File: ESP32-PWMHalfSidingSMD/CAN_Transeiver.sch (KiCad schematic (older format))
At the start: 13 parts, among them J1 RJ45, J2 RJ45, T1 + 15 in -, T2 + 15 out -, U1 TCAN332DR

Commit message: Update part numbers for ESP32-PWMHalfSidingSMD and created prelim BOM files.
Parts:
- R1, R2: Mouser Part Number 71-RN60C60R0B/R -> 71-CRCW120660R0KNAIF
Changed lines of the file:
@@
 F 2 "~" V 5780 3650 30  0000 C CNN
 F 3 "~" H 5850 3650 30  0000 C CNN
-F 4 " 71-RN60C60R0B/R" H 5850 3650 60  0001 C CNN "Mouser Part Number"
+F 4 "71-CRCW120660R0KNAIF " H 5850 3650 60  0001 C CNN "Mouser Part Number"
 	1    5850 3650
 	1    0    0    -1
@@
 F 2 "~" V 6480 3650 30  0000 C CNN
 F 3 "~" H 6550 3650 30  0000 C CNN
-F 4 " 71-RN60C60R0B/R" H 6550 3650 60  0001 C CNN "Mouser Part Number"
+F 4 "71-CRCW120660R0KNAIF " H 6550 3650 60  0001 C CNN "Mouser Part Number"
 	1    6550 3650
 	1    0    0    -1

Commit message: Updated ESP32-PWMHalfSidingSMD board.
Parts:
- C1, C3: footprint ~ -> Capacitors_SMD:C_0603; symbol C -> C-RESCUE-ESP32-PWMHalfSidingSMD
- C2: footprint ~ -> Capacitors_SMD:CP_Elec_4x5.7; symbol CP1 -> CP1-RESCUE-ESP32-PWMHalfSidingSMD
- D1, D2: footprint ~ -> Diodes_SMD:D_SMB
- J1, J2: footprint (none) -> RJ45-8N-S:RJ45_8N-S
- JP1: footprint (none) -> Pin_Headers:Pin_Header_Straight_2x02_Pitch2.54mm
- R1, R2: footprint ~ -> Resistors_SMD:R_1206; symbol R -> R-RESCUE-ESP32-PWMHalfSidingSMD
- T1, T2: footprint (none) -> Connectors_Terminal_Blocks:TerminalBlock_Pheonix_MPT-2.54mm_2pol
- U1: footprint ~ -> Housings_SOIC:SOIC-8_3.9x4.9mm_Pitch1.27mm
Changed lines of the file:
@@
 EESchema Schematic File Version 2
+LIBS:ESP32-PWMHalfSidingSMD-rescue
 LIBS:power
 LIBS:device
@@
 LIBS:memory
 LIBS:xilinx
-LIBS:special
 LIBS:microcontrollers
 LIBS:dsp
@@
 LIBS:4814p-2
 LIBS:ESP32-PWMHalfSidingSMD-cache
-EELAYER 27 0
+EELAYER 25 0
 EELAYER END
 $Descr A4 11693 8268
@@
 F 0 "U1" H 4100 3350 30  0000 C CNN
 F 1 "TCAN332DR" H 4100 3450 30  0000 C CNN
-F 2 "~" H 4100 3400 60  0000 C CNN
+F 2 "Housings_SOIC:SOIC-8_3.9x4.9mm_Pitch1.27mm" H 4100 3400 60  0001 C CNN
 F 3 "~" H 4100 3400 60  0000 C CNN
 F 4 "595-TCAN332DR" H 4100 3400 60  0001 C CNN "Mouser Part Number"
@@
 $EndComp
 $Comp
-L GND #PWR011
+L GND-RESCUE-ESP32-PWMHalfSidingSMD #PWR011
 U 1 1 5C828CBC
 P 4100 3800
@@
 	3750 3300 3750 4400
 $Comp
-L C C1
+L C-RESCUE-ESP32-PWMHalfSidingSMD C1
 U 1 1 5C828DA1
 P 4650 3800
+AR Path="/5C828DA1" Ref="C1"  Part="1"
+AR Path="/5C828AE5/5C828DA1" Ref="C1"  Part="1"
 F 0 "C1" H 4650 3900 40  0000 L CNN
 F 1 ".1 uf" H 4656 3715 40  0000 L CNN
-F 2 "~" H 4688 3650 30  0000 C CNN
+F 2 "Capacitors_SMD:C_0603" H 4688 3650 30  0001 C CNN
 F 3 "~" H 4650 3800 60  0000 C CNN
 F 4 "710-885012206095" H 4650 3800 60  0001 C CNN "Mouser Part Number"
@@
 $EndComp
 $Comp
-L CP1 C2
+L CP1-RESCUE-ESP32-PWMHalfSidingSMD C2
 U 1 1 5C828DB0
 P 5000 3800
 F 0 "C2" H 5050 3900 50  0000 L CNN
 F 1 "15 uf 15V" H 5050 3700 50  0000 L CNN
-F 2 "~" H 5000 3800 60  0000 C CNN
+F 2 "Capacitors_SMD:CP_Elec_4x5.7" H 5000 3800 60  0001 C CNN
 F 3 "~" H 5000 3800 60  0000 C CNN
 F 4 "647-UUD1C150MCL" H 5000 3800 60  0001 C CNN "Mouser Part Number"
@@
 CANL
 $Comp
-L R R1
+L R-RESCUE-ESP32-PWMHalfSidingSMD R1
 U 1 1 5C828F93
 P 5850 3650
 F 0 "R1" V 5930 3650 40  0000 C CNN
 F 1 "60 Ohms" V 5857 3651 40  0000 C CNN
-F 2 "~" V 5780 3650 30  0000 C CNN
+F 2 "Resistors_SMD:R_1206" V 5780 3650 30  0001 C CNN
 F 3 "~" H 5850 3650 30  0000 C CNN
 F 4 "71-CRCW120660R0KNAIF " H 5850 3650 60  0001 C CNN "Mouser Part Number"
@@
 $EndComp
 $Comp
-L R R2
+L R-RESCUE-ESP32-PWMHalfSidingSMD R2
 U 1 1 5C828FA2
 P 6550 3650
 F 0 "R2" V 6630 3650 40  0000 C CNN
 F 1 "60 Ohms" V 6557 3651 40  0000 C CNN
-F 2 "~" V 6480 3650 30  0000 C CNN
+F 2 "Resistors_SMD:R_1206" V 6480 3650 30  0001 C CNN
 F 3 "~" H 6550 3650 30  0000 C CNN
 F 4 "71-CRCW120660R0KNAIF " H 6550 3650 60  0001 C CNN "Mouser Part Number"
@@
 F 0 "JP1" H 6200 4350 50  0000 C CNN
 F 1 "Termination" H 6210 4070 40  0000 C CNN
-F 2 "" H 6200 4200 60  0000 C CNN
+F 2 "Pin_Headers:Pin_Header_Straight_2x02_Pitch2.54mm" H 6200 4200 60  0001 C CNN
 F 3 "" H 6200 4200 60  0000 C CNN
 F 4 "649-67997-404HLF" H 6200 4200 60  0001 C CNN "Mouser Part Number"
@@
 	6700 4150 6600 4150
 $Comp
-L C C3
+L C-RESCUE-ESP32-PWMHalfSidingSMD C3
 U 1 1 5C8290C3
 P 6200 4750
+AR Path="/5C8290C3" Ref="C3"  Part="1"
+AR Path="/5C828AE5/5C8290C3" Ref="C3"  Part="1"
 F 0 "C3" H 6200 4850 40  0000 L CNN
 F 1 "47 nf" H 6206 4665 40  0000 L CNN
-F 2 "~" H 6238 4600 30  0000 C CNN
+F 2 "Capacitors_SMD:C_0603" H 6238 4600 30  0000 C CNN
 F 3 "~" H 6200 4750 60  0000 C CNN
 F 4 "710-885012206093" H 6200 4750 60  0001 C CNN "Mouser Part Number"
@@
 $EndComp
 $Comp
-L GND #PWR012
+L GND-RESCUE-ESP32-PWMHalfSidingSMD #PWR012
 U 1 1 5C8290D2
 P 6200 5100
@@
 F 0 "J2" H 8550 5200 60  0000 C CNN
 F 1 "RJ45" H 8200 5200 60  0000 C CNN
-F 2 "" H 8350 4700 60  0000 C CNN
+F 2 "RJ45-8N-S:RJ45_8N-S" H 8350 4700 60  0001 C CNN
 F 3 "" H 8350 4700 60  0000 C CNN
 F 4 "710-615008144221" H 8350 4700 60  0001 C CNN "Mouser Part Number"
@@
 F 0 "J1" H 8550 3550 60  0000 C CNN
 F 1 "RJ45" H 8200 3550 60  0000 C CNN
-F 2 "" H 8350 3050 60  0000 C CNN
+F 2 "RJ45-8N-S:RJ45_8N-S" H 8350 3050 60  0001 C CNN
 F 3 "" H 8350 3050 60  0000 C CNN
 F 4 "710-615008144221" H 8350 3050 60  0001 C CNN "Mouser Part Number"
@@
 F 0 "T2" V 6750 2050 40  0000 C CNN
 F 1 "+ 15 out -" V 6850 2050 40  0000 C CNN
-F 2 "" H 6800 2050 60  0000 C CNN
+F 2 "Connectors_Terminal_Blocks:TerminalBlock_Pheonix_MPT-2.54mm_2pol" H 6800 2050 60  0001 C CNN
 F 3 "" H 6800 2050 60  0000 C CNN
 F 4 "651-1725656" H 6800 2050 60  0001 C CNN "Mouser Part Number"
@@
 F 0 "D2" H 6150 2050 40  0000 C CNN
 F 1 "DFLS240-7" H 6150 1850 40  0000 C CNN
-F 2 "~" H 6150 1950 60  0000 C CNN
+F 2 "Diodes_SMD:D_SMB" H 6150 1950 60  0001 C CNN
 F 3 "~" H 6150 1950 60  0000 C CNN
 F 4 "621-DFLS240-7" H 6150 1950 60  0001 C CNN "Mouser Part Number"
@@
 	7450 3000 7450 5050
 $Comp
-L GND #PWR013
+L GND-RESCUE-ESP32-PWMHalfSidingSMD #PWR013
 U 1 1 5C8295F7
 P 6750 2650
@@
 F 0 "T1" V 5800 1050 40  0000 C CNN
 F 1 "+ 15 in -" V 5900 1050 40  0000 C CNN
-F 2 "" H 5850 1050 60  0000 C CNN
+F 2 "Connectors_Terminal_Blocks:TerminalBlock_Pheonix_MPT-2.54mm_2pol" H 5850 1050 60  0001 C CNN
 F 3 "" H 5850 1050 60  0000 C CNN
 F 4 "651-1725656" H 5850 1050 60  0001 C CNN "Mouser Part Number"
@@
 F 0 "D1" H 5750 1750 40  0000 C CNN
 F 1 "DFLS240-7" H 5750 1550 40  0000 C CNN
-F 2 "~" H 5750 1650 60  0000 C CNN
+F 2 "Diodes_SMD:D_SMB" H 5750 1650 60  0001 C CNN
 F 3 "~" H 5750 1650 60  0000 C CNN
 F 4 "621-DFLS240-7" H 5750 1650 60  0001 C CNN "Mouser Part Number"
@@
 	3750 4400 3600 4400
 $Comp
-L GND #PWR014
+L GND-RESCUE-ESP32-PWMHalfSidingSMD #PWR014
 U 1 1 5C828CCB
 P 4100 4950

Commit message: Restore PocketBeagleCommandStation_SMD.kicad_pcb
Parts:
- C1, C3: footprint Capacitors_SMD:C_0603 -> ~; symbol C-RESCUE-ESP32-PWMHalfSidingSMD -> C
- C2: footprint Capacitors_SMD:CP_Elec_4x5.7 -> ~; symbol CP1-RESCUE-ESP32-PWMHalfSidingSMD -> CP1
- D1, D2: footprint Diodes_SMD:D_SMB -> ~
- J1, J2: footprint RJ45-8N-S:RJ45_8N-S -> (none)
- JP1: footprint Pin_Headers:Pin_Header_Straight_2x02_Pitch2.54mm -> (none)
- R1, R2: footprint Resistors_SMD:R_1206 -> ~; symbol R-RESCUE-ESP32-PWMHalfSidingSMD -> R
- T1, T2: footprint Connectors_Terminal_Blocks:TerminalBlock_Pheonix_MPT-2.54mm_2pol -> (none)
- U1: footprint Housings_SOIC:SOIC-8_3.9x4.9mm_Pitch1.27mm -> ~
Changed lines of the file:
@@
 EESchema Schematic File Version 2
-LIBS:ESP32-PWMHalfSidingSMD-rescue
 LIBS:power
 LIBS:device
@@
 LIBS:memory
 LIBS:xilinx
+LIBS:special
 LIBS:microcontrollers
 LIBS:dsp
@@
 LIBS:4814p-2
 LIBS:ESP32-PWMHalfSidingSMD-cache
-EELAYER 25 0
+EELAYER 27 0
 EELAYER END
 $Descr A4 11693 8268
@@
 F 0 "U1" H 4100 3350 30  0000 C CNN
 F 1 "TCAN332DR" H 4100 3450 30  0000 C CNN
-F 2 "Housings_SOIC:SOIC-8_3.9x4.9mm_Pitch1.27mm" H 4100 3400 60  0001 C CNN
+F 2 "~" H 4100 3400 60  0000 C CNN
 F 3 "~" H 4100 3400 60  0000 C CNN
 F 4 "595-TCAN332DR" H 4100 3400 60  0001 C CNN "Mouser Part Number"
@@
 $EndComp
 $Comp
-L GND-RESCUE-ESP32-PWMHalfSidingSMD #PWR011
+L GND #PWR011
 U 1 1 5C828CBC
 P 4100 3800
@@
 	3750 3300 3750 4400
 $Comp
-L C-RESCUE-ESP32-PWMHalfSidingSMD C1
+L C C1
 U 1 1 5C828DA1
 P 4650 3800
-AR Path="/5C828DA1" Ref="C1"  Part="1"
-AR Path="/5C828AE5/5C828DA1" Ref="C1"  Part="1"
 F 0 "C1" H 4650 3900 40  0000 L CNN
 F 1 ".1 uf" H 4656 3715 40  0000 L CNN
-F 2 "Capacitors_SMD:C_0603" H 4688 3650 30  0001 C CNN
+F 2 "~" H 4688 3650 30  0000 C CNN
 F 3 "~" H 4650 3800 60  0000 C CNN
 F 4 "710-885012206095" H 4650 3800 60  0001 C CNN "Mouser Part Number"
@@
 $EndComp
 $Comp
-L CP1-RESCUE-ESP32-PWMHalfSidingSMD C2
+L CP1 C2
 U 1 1 5C828DB0
 P 5000 3800
 F 0 "C2" H 5050 3900 50  0000 L CNN
 F 1 "15 uf 15V" H 5050 3700 50  0000 L CNN
-F 2 "Capacitors_SMD:CP_Elec_4x5.7" H 5000 3800 60  0001 C CNN
+F 2 "~" H 5000 3800 60  0000 C CNN
 F 3 "~" H 5000 3800 60  0000 C CNN
 F 4 "647-UUD1C150MCL" H 5000 3800 60  0001 C CNN "Mouser Part Number"
@@
 CANL
 $Comp
-L R-RESCUE-ESP32-PWMHalfSidingSMD R1
+L R R1
 U 1 1 5C828F93
 P 5850 3650
 F 0 "R1" V 5930 3650 40  0000 C CNN
 F 1 "60 Ohms" V 5857 3651 40  0000 C CNN
-F 2 "Resistors_SMD:R_1206" V 5780 3650 30  0001 C CNN
+F 2 "~" V 5780 3650 30  0000 C CNN
 F 3 "~" H 5850 3650 30  0000 C CNN
 F 4 "71-CRCW120660R0KNAIF " H 5850 3650 60  0001 C CNN "Mouser Part Number"
@@
 $EndComp
 $Comp
-L R-RESCUE-ESP32-PWMHalfSidingSMD R2
+L R R2
 U 1 1 5C828FA2
 P 6550 3650
 F 0 "R2" V 6630 3650 40  0000 C CNN
 F 1 "60 Ohms" V 6557 3651 40  0000 C CNN
-F 2 "Resistors_SMD:R_1206" V 6480 3650 30  0001 C CNN
+F 2 "~" V 6480 3650 30  0000 C CNN
 F 3 "~" H 6550 3650 30  0000 C CNN
 F 4 "71-CRCW120660R0KNAIF " H 6550 3650 60  0001 C CNN "Mouser Part Number"
@@
 F 0 "JP1" H 6200 4350 50  0000 C CNN
 F 1 "Termination" H 6210 4070 40  0000 C CNN
-F 2 "Pin_Headers:Pin_Header_Straight_2x02_Pitch2.54mm" H 6200 4200 60  0001 C CNN
+F 2 "" H 6200 4200 60  0000 C CNN
 F 3 "" H 6200 4200 60  0000 C CNN
 F 4 "649-67997-404HLF" H 6200 4200 60  0001 C CNN "Mouser Part Number"
@@
 	6700 4150 6600 4150
 $Comp
-L C-RESCUE-ESP32-PWMHalfSidingSMD C3
+L C C3
 U 1 1 5C8290C3
 P 6200 4750
-AR Path="/5C8290C3" Ref="C3"  Part="1"
-AR Path="/5C828AE5/5C8290C3" Ref="C3"  Part="1"
 F 0 "C3" H 6200 4850 40  0000 L CNN
 F 1 "47 nf" H 6206 4665 40  0000 L CNN
-F 2 "Capacitors_SMD:C_0603" H 6238 4600 30  0000 C CNN
+F 2 "~" H 6238 4600 30  0000 C CNN
 F 3 "~" H 6200 4750 60  0000 C CNN
 F 4 "710-885012206093" H 6200 4750 60  0001 C CNN "Mouser Part Number"
@@
 $EndComp
 $Comp
-L GND-RESCUE-ESP32-PWMHalfSidingSMD #PWR012
+L GND #PWR012
 U 1 1 5C8290D2
 P 6200 5100
@@
 F 0 "J2" H 8550 5200 60  0000 C CNN
 F 1 "RJ45" H 8200 5200 60  0000 C CNN
-F 2 "RJ45-8N-S:RJ45_8N-S" H 8350 4700 60  0001 C CNN
+F 2 "" H 8350 4700 60  0000 C CNN
 F 3 "" H 8350 4700 60  0000 C CNN
 F 4 "710-615008144221" H 8350 4700 60  0001 C CNN "Mouser Part Number"
@@
 F 0 "J1" H 8550 3550 60  0000 C CNN
 F 1 "RJ45" H 8200 3550 60  0000 C CNN
-F 2 "RJ45-8N-S:RJ45_8N-S" H 8350 3050 60  0001 C CNN
+F 2 "" H 8350 3050 60  0000 C CNN
 F 3 "" H 8350 3050 60  0000 C CNN
 F 4 "710-615008144221" H 8350 3050 60  0001 C CNN "Mouser Part Number"
@@
 F 0 "T2" V 6750 2050 40  0000 C CNN
 F 1 "+ 15 out -" V 6850 2050 40  0000 C CNN
-F 2 "Connectors_Terminal_Blocks:TerminalBlock_Pheonix_MPT-2.54mm_2pol" H 6800 2050 60  0001 C CNN
+F 2 "" H 6800 2050 60  0000 C CNN
 F 3 "" H 6800 2050 60  0000 C CNN
 F 4 "651-1725656" H 6800 2050 60  0001 C CNN "Mouser Part Number"
@@
 F 0 "D2" H 6150 2050 40  0000 C CNN
 F 1 "DFLS240-7" H 6150 1850 40  0000 C CNN
-F 2 "Diodes_SMD:D_SMB" H 6150 1950 60  0001 C CNN
+F 2 "~" H 6150 1950 60  0000 C CNN
 F 3 "~" H 6150 1950 60  0000 C CNN
 F 4 "621-DFLS240-7" H 6150 1950 60  0001 C CNN "Mouser Part Number"
@@
 	7450 3000 7450 5050
 $Comp
-L GND-RESCUE-ESP32-PWMHalfSidingSMD #PWR013
+L GND #PWR013
 U 1 1 5C8295F7
 P 6750 2650
@@
 F 0 "T1" V 5800 1050 40  0000 C CNN
 F 1 "+ 15 in -" V 5900 1050 40  0000 C CNN
-F 2 "Connectors_Terminal_Blocks:TerminalBlock_Pheonix_MPT-2.54mm_2pol" H 5850 1050 60  0001 C CNN
+F 2 "" H 5850 1050 60  0000 C CNN
 F 3 "" H 5850 1050 60  0000 C CNN
 F 4 "651-1725656" H 5850 1050 60  0001 C CNN "Mouser Part Number"
@@
 F 0 "D1" H 5750 1750 40  0000 C CNN
 F 1 "DFLS240-7" H 5750 1550 40  0000 C CNN
-F 2 "Diodes_SMD:D_SMB" H 5750 1650 60  0001 C CNN
+F 2 "~" H 5750 1650 60  0000 C CNN
 F 3 "~" H 5750 1650 60  0000 C CNN
 F 4 "621-DFLS240-7" H 5750 1650 60  0001 C CNN "Mouser Part Number"
@@
 	3750 4400 3600 4400
 $Comp
-L GND-RESCUE-ESP32-PWMHalfSidingSMD #PWR014
+L GND #PWR014
 U 1 1 5C828CCB
 P 4100 4950

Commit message: Repair ESP32-PWMHalfSidingSMD and generate POS file.
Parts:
- C1, C3: footprint ~ -> Capacitors_SMD:C_0603; symbol C -> C-RESCUE-ESP32-PWMHalfSidingSMD
- C2: footprint ~ -> Capacitors_SMD:CP_Elec_4x5.7; symbol CP1 -> CP1-RESCUE-ESP32-PWMHalfSidingSMD
- D1, D2: footprint ~ -> Diodes_SMD:D_SMB
- J1, J2: footprint (none) -> RJ45-8N-S:RJ45_8N-S
- JP1: footprint (none) -> Pin_Headers:Pin_Header_Angled_2x02_Pitch2.54mm
- R1, R2: footprint ~ -> Resistors_SMD:R_1206; symbol R -> R-RESCUE-ESP32-PWMHalfSidingSMD
- T1, T2: footprint (none) -> Connectors_Terminal_Blocks:TerminalBlock_Pheonix_MPT-2.54mm_2pol
- U1: footprint ~ -> (none)
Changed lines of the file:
@@
 EESchema Schematic File Version 2
+LIBS:ESP32-PWMHalfSidingSMD-rescue
 LIBS:power
 LIBS:device
@@
 LIBS:memory
 LIBS:xilinx
-LIBS:special
 LIBS:microcontrollers
 LIBS:dsp
@@
 LIBS:4814p-2
 LIBS:ESP32-PWMHalfSidingSMD-cache
-EELAYER 27 0
+EELAYER 25 0
 EELAYER END
 $Descr A4 11693 8268
@@
 F 0 "U1" H 4100 3350 30  0000 C CNN
 F 1 "TCAN332DR" H 4100 3450 30  0000 C CNN
-F 2 "~" H 4100 3400 60  0000 C CNN
+F 2 "" H 4100 3400 60  0001 C CNN
 F 3 "~" H 4100 3400 60  0000 C CNN
 F 4 "595-TCAN332DR" H 4100 3400 60  0001 C CNN "Mouser Part Number"
@@
 $EndComp
 $Comp
-L GND #PWR011
+L GND-RESCUE-ESP32-PWMHalfSidingSMD #PWR011
 U 1 1 5C828CBC
 P 4100 3800
@@
 	3750 3300 3750 4400
 $Comp
-L C C1
+L C-RESCUE-ESP32-PWMHalfSidingSMD C1
 U 1 1 5C828DA1
 P 4650 3800
+AR Path="/5C828DA1" Ref="C1"  Part="1"
+AR Path="/5C828AE5/5C828DA1" Ref="C1"  Part="1"
 F 0 "C1" H 4650 3900 40  0000 L CNN
 F 1 ".1 uf" H 4656 3715 40  0000 L CNN
-F 2 "~" H 4688 3650 30  0000 C CNN
+F 2 "Capacitors_SMD:C_0603" H 4688 3650 30  0001 C CNN
 F 3 "~" H 4650 3800 60  0000 C CNN
 F 4 "710-885012206095" H 4650 3800 60  0001 C CNN "Mouser Part Number"
@@
 $EndComp
 $Comp
-L CP1 C2
+L CP1-RESCUE-ESP32-PWMHalfSidingSMD C2
 U 1 1 5C828DB0
 P 5000 3800
 F 0 "C2" H 5050 3900 50  0000 L CNN
 F 1 "15 uf 15V" H 5050 3700 50  0000 L CNN
-F 2 "~" H 5000 3800 60  0000 C CNN
+F 2 "Capacitors_SMD:CP_Elec_4x5.7" H 5000 3800 60  0001 C CNN
 F 3 "~" H 5000 3800 60  0000 C CNN
 F 4 "647-UUD1C150MCL" H 5000 3800 60  0001 C CNN "Mouser Part Number"
@@
 CANL
 $Comp
-L R R1
+L R-RESCUE-ESP32-PWMHalfSidingSMD R1
 U 1 1 5C828F93
 P 5850 3650
 F 0 "R1" V 5930 3650 40  0000 C CNN
 F 1 "60 Ohms" V 5857 3651 40  0000 C CNN
-F 2 "~" V 5780 3650 30  0000 C CNN
+F 2 "Resistors_SMD:R_1206" V 5780 3650 30  0001 C CNN
 F 3 "~" H 5850 3650 30  0000 C CNN
 F 4 "71-CRCW120660R0KNAIF " H 5850 3650 60  0001 C CNN "Mouser Part Number"
@@
 $EndComp
 $Comp
-L R R2
+L R-RESCUE-ESP32-PWMHalfSidingSMD R2
 U 1 1 5C828FA2
 P 6550 3650
 F 0 "R2" V 6630 3650 40  0000 C CNN
 F 1 "60 Ohms" V 6557 3651 40  0000 C CNN
-F 2 "~" V 6480 3650 30  0000 C CNN
+F 2 "Resistors_SMD:R_1206" V 6480 3650 30  0001 C CNN
 F 3 "~" H 6550 3650 30  0000 C CNN
 F 4 "71-CRCW120660R0KNAIF " H 6550 3650 60  0001 C CNN "Mouser Part Number"
@@
 F 0 "JP1" H 6200 4350 50  0000 C CNN
 F 1 "Termination" H 6210 4070 40  0000 C CNN
-F 2 "" H 6200 4200 60  0000 C CNN
+F 2 "Pin_Headers:Pin_Header_Angled_2x02_Pitch2.54mm" H 6200 4200 60  0001 C CNN
 F 3 "" H 6200 4200 60  0000 C CNN
 F 4 "649-67997-404HLF" H 6200 4200 60  0001 C CNN "Mouser Part Number"
@@
 	6700 4150 6600 4150
 $Comp
-L C C3
+L C-RESCUE-ESP32-PWMHalfSidingSMD C3
 U 1 1 5C8290C3
 P 6200 4750
+AR Path="/5C8290C3" Ref="C3"  Part="1"
+AR Path="/5C828AE5/5C8290C3" Ref="C3"  Part="1"
 F 0 "C3" H 6200 4850 40  0000 L CNN
 F 1 "47 nf" H 6206 4665 40  0000 L CNN
-F 2 "~" H 6238 4600 30  0000 C CNN
+F 2 "Capacitors_SMD:C_0603" H 6238 4600 30  0000 C CNN
 F 3 "~" H 6200 4750 60  0000 C CNN
 F 4 "710-885012206093" H 6200 4750 60  0001 C CNN "Mouser Part Number"
@@
 $EndComp
 $Comp
-L GND #PWR012
+L GND-RESCUE-ESP32-PWMHalfSidingSMD #PWR012
 U 1 1 5C8290D2
 P 6200 5100
@@
 F 0 "J2" H 8550 5200 60  0000 C CNN
 F 1 "RJ45" H 8200 5200 60  0000 C CNN
-F 2 "" H 8350 4700 60  0000 C CNN
+F 2 "RJ45-8N-S:RJ45_8N-S" H 8350 4700 60  0001 C CNN
 F 3 "" H 8350 4700 60  0000 C CNN
 F 4 "710-615008144221" H 8350 4700 60  0001 C CNN "Mouser Part Number"
@@
 F 0 "J1" H 8550 3550 60  0000 C CNN
 F 1 "RJ45" H 8200 3550 60  0000 C CNN
-F 2 "" H 8350 3050 60  0000 C CNN
+F 2 "RJ45-8N-S:RJ45_8N-S" H 8350 3050 60  0001 C CNN
 F 3 "" H 8350 3050 60  0000 C CNN
 F 4 "710-615008144221" H 8350 3050 60  0001 C CNN "Mouser Part Number"
@@
 F 0 "T2" V 6750 2050 40  0000 C CNN
 F 1 "+ 15 out -" V 6850 2050 40  0000 C CNN
-F 2 "" H 6800 2050 60  0000 C CNN
+F 2 "Connectors_Terminal_Blocks:TerminalBlock_Pheonix_MPT-2.54mm_2pol" H 6800 2050 60  0001 C CNN
 F 3 "" H 6800 2050 60  0000 C CNN
 F 4 "651-1725656" H 6800 2050 60  0001 C CNN "Mouser Part Number"
@@
 F 0 "D2" H 6150 2050 40  0000 C CNN
 F 1 "DFLS240-7" H 6150 1850 40  0000 C CNN
-F 2 "~" H 6150 1950 60  0000 C CNN
+F 2 "Diodes_SMD:D_SMB" H 6150 1950 60  0001 C CNN
 F 3 "~" H 6150 1950 60  0000 C CNN
 F 4 "621-DFLS240-7" H 6150 1950 60  0001 C CNN "Mouser Part Number"
@@
 	7450 3000 7450 5050
 $Comp
-L GND #PWR013
+L GND-RESCUE-ESP32-PWMHalfSidingSMD #PWR013
 U 1 1 5C8295F7
 P 6750 2650
@@
 F 0 "T1" V 5800 1050 40  0000 C CNN
 F 1 "+ 15 in -" V 5900 1050 40  0000 C CNN
-F 2 "" H 5850 1050 60  0000 C CNN
+F 2 "Connectors_Terminal_Blocks:TerminalBlock_Pheonix_MPT-2.54mm_2pol" H 5850 1050 60  0001 C CNN
 F 3 "" H 5850 1050 60  0000 C CNN
 F 4 "651-1725656" H 5850 1050 60  0001 C CNN "Mouser Part Number"
@@
 F 0 "D1" H 5750 1750 40  0000 C CNN
 F 1 "DFLS240-7" H 5750 1550 40  0000 C CNN
-F 2 "~" H 5750 1650 60  0000 C CNN
+F 2 "Diodes_SMD:D_SMB" H 5750 1650 60  0001 C CNN
 F 3 "~" H 5750 1650 60  0000 C CNN
 F 4 "621-DFLS240-7" H 5750 1650 60  0001 C CNN "Mouser Part Number"
@@
 	3750 4400 3600 4400
 $Comp
-L GND #PWR014
+L GND-RESCUE-ESP32-PWMHalfSidingSMD #PWR014
 U 1 1 5C828CCB
 P 4100 4950

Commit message: Generate BOM for ESP32-PWMHalfSidingSMD.
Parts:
- R1, R2: Mouser Part Number 71-CRCW120660R0KNAIF -> 71-CRCW120660R0KNAIF
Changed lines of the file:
@@
 F 2 "Resistors_SMD:R_1206" V 5780 3650 30  0001 C CNN
 F 3 "~" H 5850 3650 30  0000 C CNN
-F 4 "71-CRCW120660R0KNAIF " H 5850 3650 60  0001 C CNN "Mouser Part Number"
+F 4 "71-CRCW120660R0KNAIF" H 5850 3650 60  0001 C CNN "Mouser Part Number"
 	1    5850 3650
 	1    0    0    -1
@@
 F 2 "Resistors_SMD:R_1206" V 6480 3650 30  0001 C CNN
 F 3 "~" H 6550 3650 30  0000 C CNN
-F 4 "71-CRCW120660R0KNAIF " H 6550 3650 60  0001 C CNN "Mouser Part Number"
+F 4 "71-CRCW120660R0KNAIF" H 6550 3650 60  0001 C CNN "Mouser Part Number"
 	1    6550 3650
 	1    0    0    -1

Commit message: Update footprints in ESP32-PWMHalfSidingSMD.
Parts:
- U1: footprint (none) -> Housings_SOIC:SOIC-8_3.9x4.9mm_Pitch1.27mm
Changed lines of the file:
@@
 F 0 "U1" H 4100 3350 30  0000 C CNN
 F 1 "TCAN332DR" H 4100 3450 30  0000 C CNN
-F 2 "" H 4100 3400 60  0001 C CNN
+F 2 "Housings_SOIC:SOIC-8_3.9x4.9mm_Pitch1.27mm" H 4100 3400 60  0001 C CNN
 F 3 "~" H 4100 3400 60  0000 C CNN
 F 4 "595-TCAN332DR" H 4100 3400 60  0001 C CNN "Mouser Part Number"

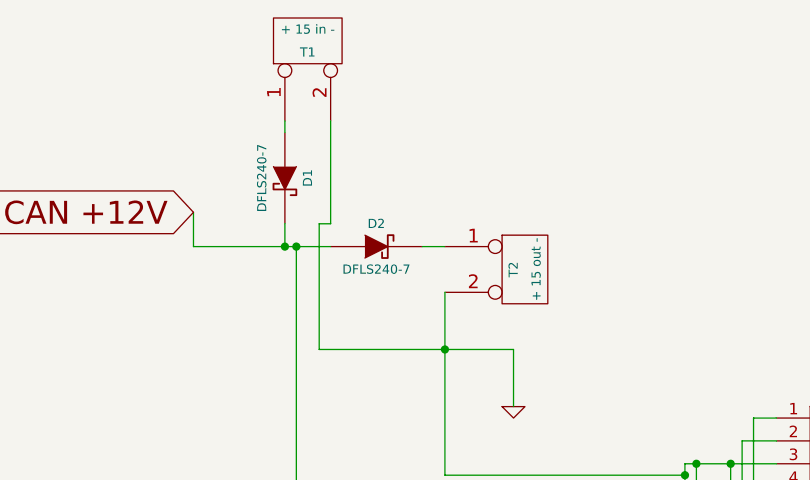
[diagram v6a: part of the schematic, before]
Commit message: Add 3D files for the through hole parts and update documenation for ESP32-PWMHalfSidingSMD.
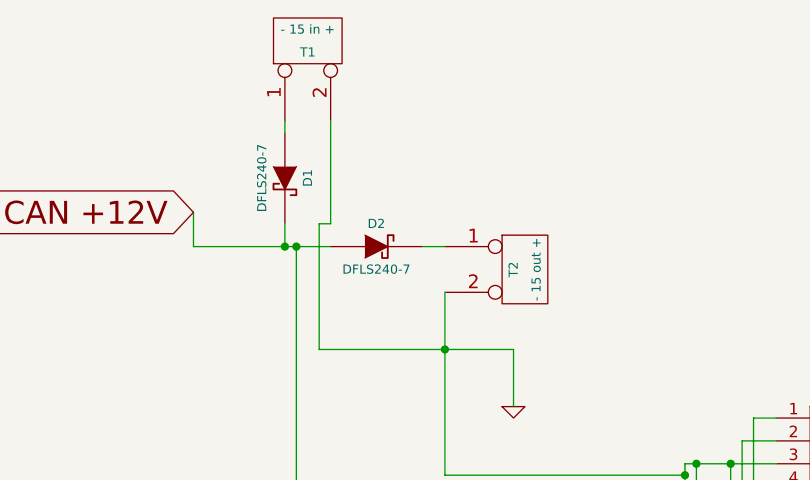
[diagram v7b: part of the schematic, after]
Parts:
- T1: value + 15 in - -> - 15 in +
- T2: value + 15 out - -> - 15 out +
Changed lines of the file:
@@
 P 6800 2050
 F 0 "T2" V 6750 2050 40  0000 C CNN
-F 1 "+ 15 out -" V 6850 2050 40  0000 C CNN
+F 1 "- 15 out +" V 6850 2050 40  0000 C CNN
 F 2 "Connectors_Terminal_Blocks:TerminalBlock_Pheonix_MPT-2.54mm_2pol" H 6800 2050 60  0001 C CNN
 F 3 "" H 6800 2050 60  0000 C CNN
@@
 P 5850 1050
 F 0 "T1" V 5800 1050 40  0000 C CNN
-F 1 "+ 15 in -" V 5900 1050 40  0000 C CNN
+F 1 "- 15 in +" V 5900 1050 40  0000 C CNN
 F 2 "Connectors_Terminal_Blocks:TerminalBlock_Pheonix_MPT-2.54mm_2pol" H 5850 1050 60  0001 C CNN
 F 3 "" H 5850 1050 60  0000 C CNN
